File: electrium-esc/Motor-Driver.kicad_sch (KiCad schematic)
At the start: 0 parts

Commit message: Complete Motor Driver!
Put in place passive components per documentation
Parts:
- added C? (x8): 10u, symbol Device:C
- added C? (x4): 0.1u, symbol Device:C
- added C? (x2): 1u, symbol Device:C
- added C? (x2): 1n, symbol Device:C
- added C?: 2.2u, symbol Device:C
- added C? (x2): 15u, symbol Device:C
- added C?: 47u, symbol Device:C_Polarized
- added C?: 6.8n, symbol Device:C
- added C?: 22n, symbol Device:C
- added C?: 120p, symbol Device:C
- added D?: 1N5819, Diode_THT:D_DO-41_SOD81_P10.16mm_Horizontal, symbol Diode:1N5819
- added L?: 22u, symbol pspice:INDUCTOR
- added R?: 15k, symbol Device:R
- added R? (x3): 10k, symbol Device:R
- added R? (x4): 100, symbol Device:R
- added R?: 220k, symbol Device:R
- added R? (x3): 2k2, symbol Device:R
- added R? (x3): 39k, symbol Device:R
- added R?: 31k6, symbol Device:R
- added U?: DRV8301DCAR, SOP50P810X120-57N, symbol DRV8301DCAR:DRV8301DCAR
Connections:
- new net: C?.1, U?.38 (BST_C)
- new net: C?.1, D?.1 (K), L?.1, U?.50 (PH_1), U?.51 (PH_2)
- new net: C?.1, R?.2, U?.31 (SN2)
- new net: C?.2, R?.2, U?.30 (SP2)
- new net: C?.1, U?.43 (BST_B)
- new net: R?.2, U?.1 (RT_CLK)
- new net: C?.1, R?.2, U?.33 (SN1)
- new net: C?.2, R?.2, U?.32 (SP1)
- new net: C?.2, U?.52 (BST_BK)
- new net: C?.2, U?.14 (CP1)
- new net: C?.1, U?.15 (CP2)
- new net: C?.1, U?.48 (BST_A)
- new net +3.3V: C?.1, L?.2, R?.1, R?.1, U?.24 (REF), U?.49 (VDD_SPI)
- new net AVDD: C?.1, U?.27 (AVDD)
- new net BR_SO1: U?.25 (SO1)
- new net BR_SO2: U?.26 (SO2)
- new net COMP: C?.2, R?.1, U?.2 (COMP)
- new net DC_CAL: U?.12 (DC_CAL)
- new net DTC: R?.2, U?.7 (DTC)
- new net DVDD: C?.2, U?.23 (DVDD)
- new net EN_GATE: U?.16 (EN_GATE)
- new net GND: C?.1, C?.1, C?.1, C?.1, C?.1, C?.2, C?.2, C?.2, C?.2, C?.2, C?.2, C?.2, C?.2, C?.2, C?.2, C?.2, D?.2 (A), R?.1, R?.1, R?.1, R?.1, R?.1, R?.2, U?.28 (AGND), U?.57 (EP)
- new net GVDD: C?.2, U?.13 (GVDD)
- new net H1: U?.17 (INH_A)
- new net H1_LOW: U?.44 (SL_A)
- new net H1_VS: C?.2, R?.2, U?.46 (SH_A)
- new net H2: U?.19 (INH_B)
- new net H2_LOW: U?.39 (SL_B)
- new net H2_VS: C?.2, R?.2, U?.41 (SH_B)
- new net H3: U?.21 (INH_C)
- new net H3_LOW: U?.34 (SL_C)
- new net H3_VS: C?.2, R?.2, U?.36 (SH_C)
- new net L1: U?.18 (INL_A)
- new net L2: U?.20 (INL_B)
- new net L3: U?.22 (INL_C)
- new net M_H1: U?.47 (GH_A)
- new net M_H2: U?.42 (GH_B)
- new net M_H3: U?.37 (GH_C)
- new net M_L1: U?.45 (GL_A)
- new net M_L2: U?.40 (GL_B)
- new net M_L3: U?.35 (GL_C)
- new net NFAULT: R?.2, U?.6 (N_FAULT)
- new net SCLK: U?.11 (SCLK)
- new net SCS: U?.8 (N_SCS)
- new net SD0: U?.10 (SDO)
- new net SDI: U?.9 (SDI)
- new net SENS1: R?.1, R?.2
- new net SENS2: R?.1, R?.2
- new net SENS3: R?.1, R?.2
- new net SH1_A: R?.1
- new net SH1_B: R?.1
- new net SH2_A: R?.1
- new net SH2_B: R?.1
- new net VSENSE: R?.1, R?.2, U?.3 (VSENSE)
- new net V_SUPPLY: C?.1, C?.1, C?.1, C?.1, C?.1, C?.1, C?.1, C?.1, C?.1, C?.2, U?.29 (PVDD1), U?.53 (PVDD2_1), U?.54 (PVDD2_2)
- no-connect marks 0 -> 4
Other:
- note added: "Caps will need to withstand 50V soldered directly to battery line"
- note added: "Decoupling Capacitors"
- note added: "MCU Sense Circuity"
- note added: "Need to read documentation more, can I just directly make this 3.3V or do I need a regulator?"

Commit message: Modify title
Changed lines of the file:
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@@
     (effects (font (size 1.27 1.27)) (justify left))
   )
-  (hierarchical_label "SD0" (shape input) (at 114.3 92.71 180)
+  (hierarchical_label "SD0" (shape output) (at 114.3 92.71 180)
     (effects (font (size 1.27 1.27)) (justify right))
   )

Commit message: Fix Error
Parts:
- C26, C27, C28, C29, C30, C31, C32, C33, C34, C35, C36, C37, C38, C39, C40, C42, C43, C44, C45, C46, C47, C48: renamed from C?; footprint (none) -> Capacitor_SMD:C_0603_1608Metric
- C41: renamed from C?; footprint (none) -> Capacitor_THT:CP_Radial_D10.0mm_P5.00mm
- L1: renamed from L?; footprint (none) -> Inductor_SMD:L_Wuerth_HCI-1335
- R16, R17, R18, R19, R20, R21, R22, R23, R24, R25, R26, R27, R28, R29, R30, R31: renamed from R?; footprint (none) -> Resistor_SMD:R_0603_1608Metric
- gave numbers to parts that had none: 2
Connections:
- net at R18.2: now also C29.2
- net at D3.1 (K), L1.1, U2.50 (PH_1)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: now also C33.2; no longer C33.1
- net at U2.52 (BST_BK): now also C33.1; no longer C33.2
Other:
- moved on the sheet: C33

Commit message: Update Footprints for schematic symbols
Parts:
- U2: footprint SOP50P810X120-57N -> Package_SO:HTSSOP-56-1EP_6.1x14mm_P0.5mm_EP3.61x6.35mm
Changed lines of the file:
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@@
     (property "Reference" "U2" (id 0) (at 143.51 64.77 0))
     (property "Value" "DRV8301DCAR" (id 1) (at 139.7 147.32 0))
-    (property "Footprint" "SOP50P810X120-57N" (id 2) (at 146.05 67.31 0)
+    (property "Footprint" "Package_SO:HTSSOP-56-1EP_6.1x14mm_P0.5mm_EP3.61x6.35mm" (id 2) (at 146.05 67.31 0)
       (effects (font (size 1.27 1.27)) (justify left) hide)
     )

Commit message: Update footprints
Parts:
- C41: footprint Capacitor_THT:CP_Radial_D10.0mm_P5.00mm -> Capacitor_THT:CP_Radial_D4.0mm_P1.50mm
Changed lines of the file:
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@@
       (effects (font (size 1.27 1.27)) (justify left))
     )
-    (property "Footprint" "Capacitor_THT:CP_Radial_D10.0mm_P5.00mm" (id 2) (at 201.6252 90.17 0)
+    (property "Footprint" "Capacitor_THT:CP_Radial_D4.0mm_P1.50mm" (id 2) (at 201.6252 90.17 0)
       (effects (font (size 1.27 1.27)) hide)
     )

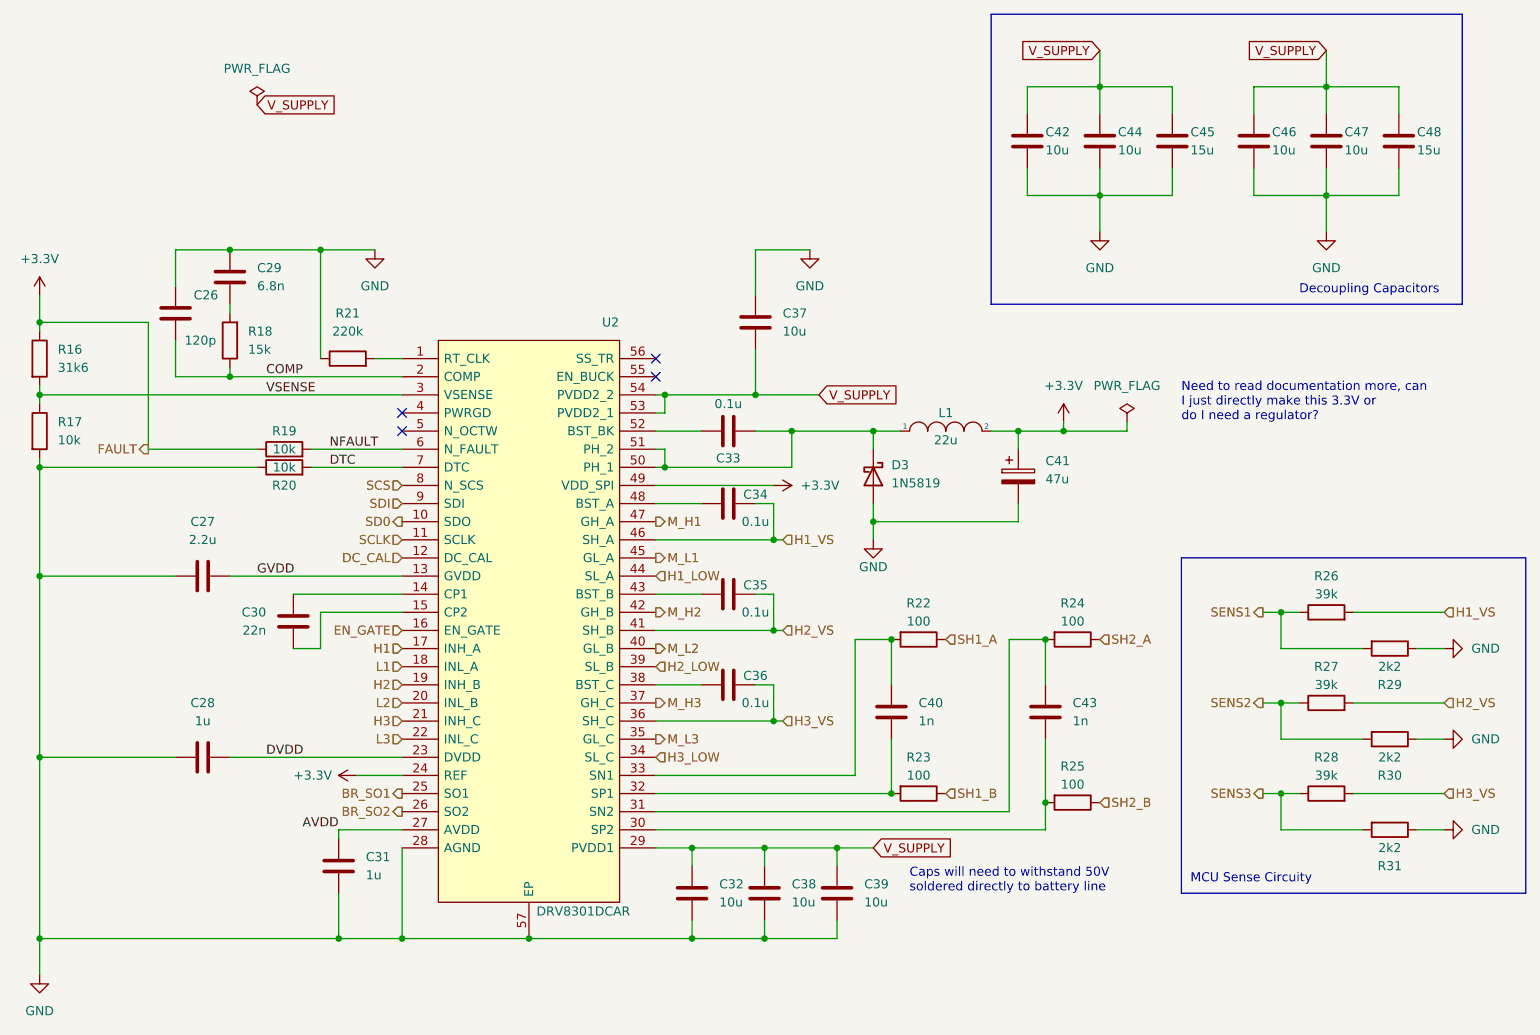
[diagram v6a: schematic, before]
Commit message: relabel components to make more sense
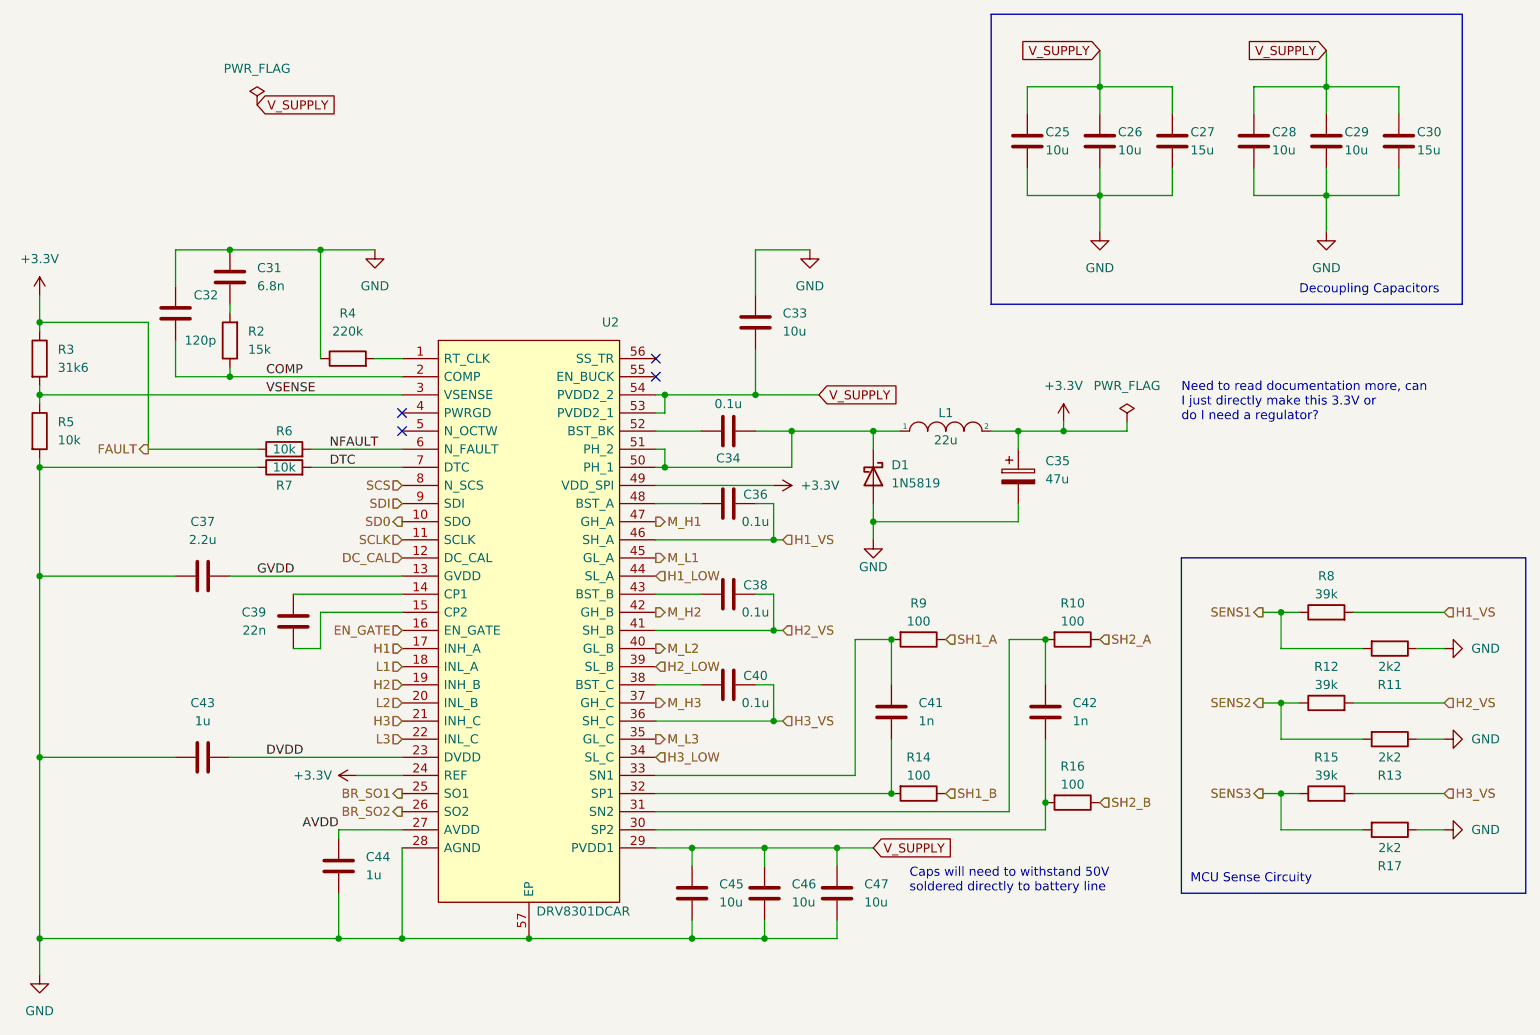
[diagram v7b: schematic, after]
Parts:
- renumbered C42 to C25, C44 to C26, C45 to C27, C46 to C28, C47 to C29, C48 to C30, C29 to C31, C26 to C32, C37 to C33, C33 to C34, C41 to C35, C34 to C36, C27 to C37, C35 to C38, C30 to C39, C36 to C40, C40 to C41, C43 to C42, C28 to C43, C31 to C44, C32 to C45, C38 to C46, C39 to C47, D3 to D1, R24 to R10, R29 to R11, R27 to R12, R30 to R13, R23 to R14, R28 to R15, R25 to R16, R31 to R17, R18 to R2, R16 to R3, R21 to R4, R17 to R5, R19 to R6, R20 to R7, R26 to R8, R22 to R9

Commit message: Change to cheaper mosfets
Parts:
- L1: footprint Inductor_SMD:L_Wuerth_HCI-1335 -> Inductor_SMD:L_Vishay_IHLP-2020
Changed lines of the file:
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@@
     (property "Reference" "L1" (id 0) (at 190.5 77.47 0))
     (property "Value" "22u" (id 1) (at 190.5 81.28 0))
-    (property "Footprint" "Inductor_SMD:L_Wuerth_HCI-1335" (id 2) (at 190.5 80.01 0)
+    (property "Footprint" "Inductor_SMD:L_Vishay_IHLP-2020" (id 2) (at 190.5 80.01 0)
       (effects (font (size 1.27 1.27)) hide)
     )
